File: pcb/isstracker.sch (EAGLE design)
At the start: 23 parts, among them IC1 74LS125N, J1 MOTOR_RIGHT, J2 CONTROL, J3 MOTOR_LEFT, J4 DISPLAY, J5 DEC_POSITION, J7 LED, J8 UART, J9 DISTANCE, U1 ARGON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

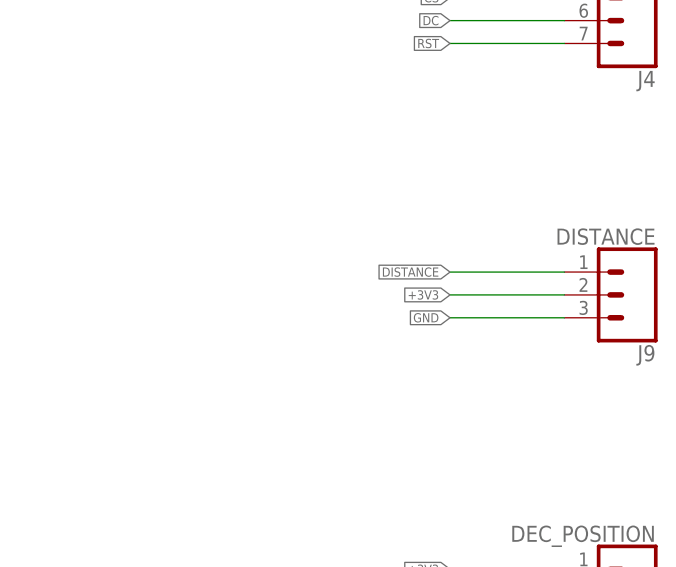
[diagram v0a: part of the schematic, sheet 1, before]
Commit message: Fixing PCB to use the new IR sensor instead.
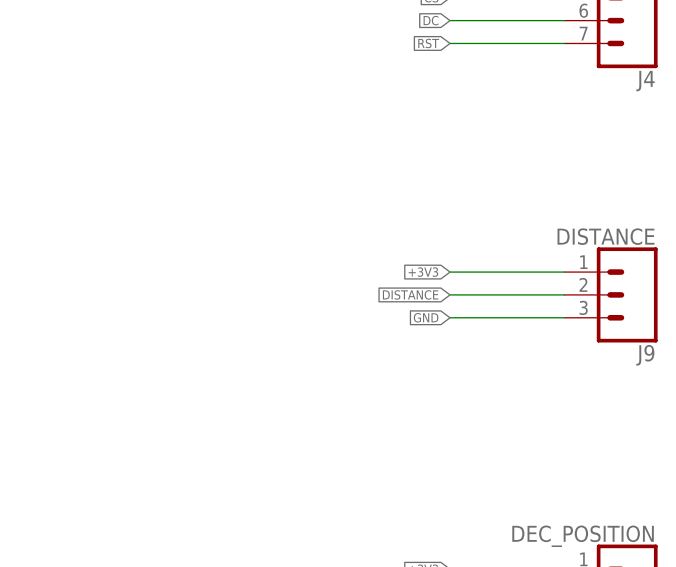
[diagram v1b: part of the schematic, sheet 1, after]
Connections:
- net +3V3: now also J9.1; no longer J9.2
- net DISTANCE: now also J9.2; no longer J9.1
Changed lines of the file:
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@@
 </segment>
 <segment>
-<wire x1="251.46" y1="147.32" x2="238.76" y2="147.32" width="0.1524" layer="91"/>
-<label x="238.76" y="147.32" size="1.016" layer="95" rot="R180" xref="yes"/>
-<pinref part="J9" gate="J$1" pin="2"/>
+<wire x1="251.46" y1="149.86" x2="238.76" y2="149.86" width="0.1524" layer="91"/>
+<label x="238.76" y="149.86" size="1.016" layer="95" rot="R180" xref="yes"/>
+<pinref part="J9" gate="J$1" pin="1"/>
 </segment>
 </net>
@@
 <net name="DISTANCE" class="0">
 <segment>
-<wire x1="251.46" y1="149.86" x2="238.76" y2="149.86" width="0.1524" layer="91"/>
-<label x="238.76" y="149.86" size="1.016" layer="95" rot="R180" xref="yes"/>
-<pinref part="J9" gate="J$1" pin="1"/>
-</segment>
-<segment>
 <pinref part="U1" gate="U1" pin="A2"/>
 <wire x1="124.46" y1="180.34" x2="114.3" y2="180.34" width="0.1524" layer="91"/>
 <label x="114.3" y="180.34" size="1.016" layer="95" rot="R180" xref="yes"/>
 </segment>
+<segment>
+<wire x1="251.46" y1="147.32" x2="238.76" y2="147.32" width="0.1524" layer="91"/>
+<label x="238.76" y="147.32" size="1.016" layer="95" rot="R180" xref="yes"/>
+<pinref part="J9" gate="J$1" pin="2"/>
+</segment>
 </net>

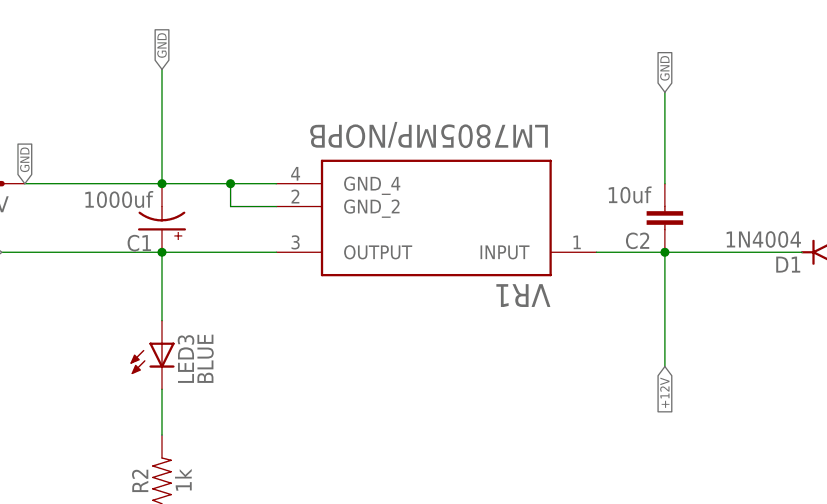
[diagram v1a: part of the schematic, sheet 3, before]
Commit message: Version 47:
* Only wake motor from sleep IFF we are going to move the motor
* Clean up some extra logging
* Add LED controls for the globe lighting
* This includes the first PCB sent out for production at OSHPark
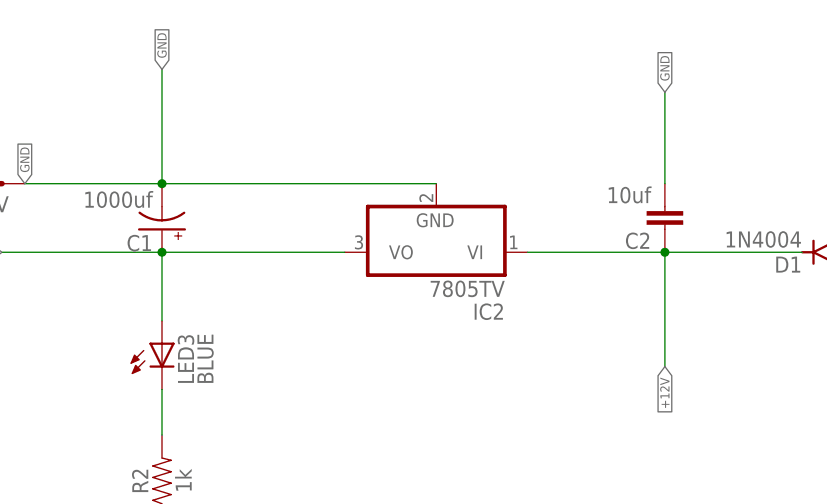
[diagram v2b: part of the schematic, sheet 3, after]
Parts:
- removed VR1: LM7805MP/NOPB, LM7805MP_NOPB:LM7805MP/NOPB
- added IC2: 7805TV, linear:7805TV
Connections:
- net +12V: now also IC2.VI; no longer VR1.INPUT
- net +5V: now also IC2.VO; no longer VR1.OUTPUT
- net GND: now also IC2.GND; no longer VR1.GND_2, VR1.GND_4
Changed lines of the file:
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@@
 <part name="R2" library="SparkFun-Resistors" library_urn="urn:adsk.eagle:library:532" deviceset="0.3OHM" device="-0805-1/8W-1%" package3d_urn="urn:adsk.eagle:package:39651/1" value="1k"/>
 <part name="J5" library="SparkFun-Connectors" library_urn="urn:adsk.eagle:library:513" deviceset="CONN_03" device="" package3d_urn="urn:adsk.eagle:package:38063/1" value="DEC_POSITION"/>
-<part name="VR1" library="LM7805MP_NOPB" deviceset="LM7805MP/NOPB" device=""/>
 <part name="C2" library="SparkFun-Capacitors" library_urn="urn:adsk.eagle:library:510" deviceset="1.0UF" device="-0805-25V-10%" package3d_urn="urn:adsk.eagle:package:37429/1" value="10uf"/>
 <part name="J4" library="SparkFun-Connectors" library_urn="urn:adsk.eagle:library:513" deviceset="CONN_07" device="" package3d_urn="urn:adsk.eagle:package:38129/1" value="DISPLAY"/>
@@
 <part name="H3" library="holes" library_urn="urn:adsk.eagle:library:237" deviceset="MOUNT-HOLE" device="3.0" package3d_urn="urn:adsk.eagle:package:14277/1"/>
 <part name="H4" library="holes" library_urn="urn:adsk.eagle:library:237" deviceset="MOUNT-HOLE" device="3.0" package3d_urn="urn:adsk.eagle:package:14277/1"/>
+<part name="IC2" library="linear" library_urn="urn:adsk.eagle:library:262" deviceset="78*" device="TV" package3d_urn="urn:adsk.eagle:package:16417/2" technology="05"/>
 </parts>
 <sheets>
@@
 <attribute name="VALUE" x="47.244" y="101.6" size="1.778" layer="96" font="vector" rot="R90" align="top-center"/>
 </instance>
-<instance part="VR1" gate="G$1" x="76.2" y="129.54" smashed="yes" rot="R180">
-<attribute name="NAME" x="88.9" y="123.46" size="2.54" layer="95" ratio="10" rot="SR180"/>
-<attribute name="VALUE" x="88.9" y="138.62" size="2.54" layer="96" ratio="10" rot="SR180" align="top-left"/>
-</instance>
 <instance part="C2" gate="G$1" x="101.6" y="132.08" smashed="yes" rot="R180">
 <attribute name="NAME" x="100.076" y="129.159" size="1.778" layer="95" font="vector" rot="R180"/>
@@
 <attribute name="NAME" x="116.84" y="126.5174" size="1.778" layer="95" rot="R180"/>
 <attribute name="VALUE" x="116.84" y="129.3114" size="1.778" layer="96" rot="R180"/>
+</instance>
+<instance part="IC2" gate="A1" x="76.2" y="127" smashed="yes" rot="R180">
+<attribute name="NAME" x="83.82" y="121.285" size="1.778" layer="95" rot="R180"/>
+<attribute name="VALUE" x="83.82" y="123.825" size="1.778" layer="96" rot="R180"/>
 </instance>
 </instances>
@@
 <net name="+5V" class="0">
 <segment>
-<pinref part="VR1" gate="G$1" pin="OUTPUT"/>
 <pinref part="C1" gate="G$1" pin="+"/>
-<wire x1="58.42" y1="127" x2="45.72" y2="127" width="0.1524" layer="91"/>
+<wire x1="66.04" y1="127" x2="45.72" y2="127" width="0.1524" layer="91"/>
 <wire x1="45.72" y1="127" x2="27.94" y2="127" width="0.1524" layer="91"/>
 <junction x="45.72" y="127"/>
@@
 <wire x1="45.72" y1="127" x2="45.72" y2="119.38" width="0.1524" layer="91"/>
 <label x="27.94" y="127" size="1.016" layer="95" rot="R180" xref="yes"/>
+<pinref part="IC2" gate="A1" pin="VO"/>
 </segment>
 </net>
 <net name="GND" class="0">
 <segment>
-<pinref part="VR1" gate="G$1" pin="GND_2"/>
-<wire x1="58.42" y1="132.08" x2="53.34" y2="132.08" width="0.1524" layer="91"/>
-<wire x1="53.34" y1="132.08" x2="53.34" y2="134.62" width="0.1524" layer="91"/>
 <pinref part="C1" gate="G$1" pin="-"/>
-<wire x1="53.34" y1="134.62" x2="45.72" y2="134.62" width="0.1524" layer="91"/>
-<pinref part="VR1" gate="G$1" pin="GND_4"/>
-<wire x1="58.42" y1="134.62" x2="53.34" y2="134.62" width="0.1524" layer="91"/>
-<junction x="53.34" y="134.62"/>
 <pinref part="X1" gate="-2" pin="S"/>
 <wire x1="45.72" y1="134.62" x2="30.48" y2="134.62" width="0.1524" layer="91"/>
@@
 <label x="45.72" y="147.32" size="1.016" layer="95" rot="R90" xref="yes"/>
 <label x="30.48" y="134.62" size="1.016" layer="95" rot="R90" xref="yes"/>
+<pinref part="IC2" gate="A1" pin="GND"/>
+<wire x1="45.72" y1="134.62" x2="76.2" y2="134.62" width="0.1524" layer="91"/>
 </segment>
 <segment>
@@
 <pinref part="C2" gate="G$1" pin="1"/>
 <wire x1="116.84" y1="127" x2="101.6" y2="127" width="0.1524" layer="91"/>
-<pinref part="VR1" gate="G$1" pin="INPUT"/>
-<wire x1="101.6" y1="127" x2="93.98" y2="127" width="0.1524" layer="91"/>
 <junction x="101.6" y="127"/>
 <wire x1="101.6" y1="127" x2="101.6" y2="114.3" width="0.1524" layer="91"/>
 <label x="101.6" y="114.3" size="1.016" layer="95" rot="R270" xref="yes"/>
-</segment>
-</net>
+<pinref part="IC2" gate="A1" pin="VI"/>
+<wire x1="101.6" y1="127" x2="86.36" y2="127" width="0.1524" layer="91"/>
+</segment>
+</net>

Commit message: Updating to the latest PCB to fix breaking issues
* Fixed capacitor sets for both boards to be larger and polarized on the
LDO's
* Fixed left track for motor board as it was 1 pin too short
* Switched from Declination to Azimuth
* Moved Azimuth signaling to the internal board to allow for movement
* Removed resistors on 5V LED signal buffer
* Switch LED pinout to match the Lumenati ordering
* Internal board got a polarized capacitor
* Internal board layout moved around to better match reality
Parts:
- removed J5: DEC_POSITION, SparkFun-Connectors:CONN_03
- removed R3: 300, SparkFun-Resistors:0.3OHM-0805-1/8W-1%
- added LED1: RED, adafruit:LED3MM
- C1: value 1000uf -> 100uF; device SparkFun-Capacitors:1000UF-RADIAL-5MM-25V-20% -> SparkFun-Capacitors:100UF-POLAR-RADIAL-2.5MM-25V-20%
- C2: value 10uf -> 100uF; device SparkFun-Capacitors:1.0UF-0805-25V-10% -> SparkFun-Capacitors:100UF-POLAR-RADIAL-2.5MM-25V-20%
- H1, H2, H3, H4: value MOUNT-HOLE3.0 -> STAND-OFF; device holes:MOUNT-HOLE3.0 -> SparkFun-Hardware:STAND-OFF
- IC1: value 74LS125N -> SN74AHCT125N; device adafruit:74LS125N -> adafruit:74125N
- IC2: value 7805TV -> L7805CV
- J2: value CONTROL -> MOTOR_LEFT; device SparkFun-Connectors:CONN_08" -> SparkFun-Connectors:CONN_11
- J3: value MOTOR_LEFT -> CONTROL; device SparkFun-Connectors:CONN_10" -> SparkFun-Connectors:CONN_08"
- R1: value 300 -> 1k
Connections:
- removed net DEC: J5.3, U1.A1
- removed net N$3: J7.1, R3.1
- new net AZIMUTH: J3.8, U1.A1
- net +12V: now also C2.+, R1.2; no longer C2.1
- net +3V3: no longer J5.1
- net +5V: now also J3.5; no longer J1.13, J1.14, J2.3
- net A+: now also J3.4; no longer J2.7
- net A-: now also J3.3; no longer J2.6
- net B+: now also J3.2; no longer J2.5
- net B-: now also J3.1; no longer J2.4
- net CO: now also IC1A.O, J7.2; no longer IC1D.O, R1.2
- net DO: now also IC1B.O, J7.3; no longer IC1C.O, R3.2
- net GND: now also C2.-, IC1C.O, IC1D.O, J2.3, J3.6, J7.1, LED1.C; no longer C2.2, IC1A.O, IC1B.O, J2.2, J3.3, J5.2, J7.3
- net LED_CO: now also IC1A.I; no longer IC1D.I
- net LED_DO: now also IC1B.I; no longer IC1C.I
- net MTR_DIR: now also J2.1; no longer J3.1
- net MTR_MS1: now also J2.10; no longer J3.9
- net MTR_SLP: now also J2.11; no longer J3.10
- net MTR_STEP: now also J2.2; no longer J3.2
- net N$2: now also LED1.A; no longer J7.2
- net SERVO: now also J3.7; no longer J2.8

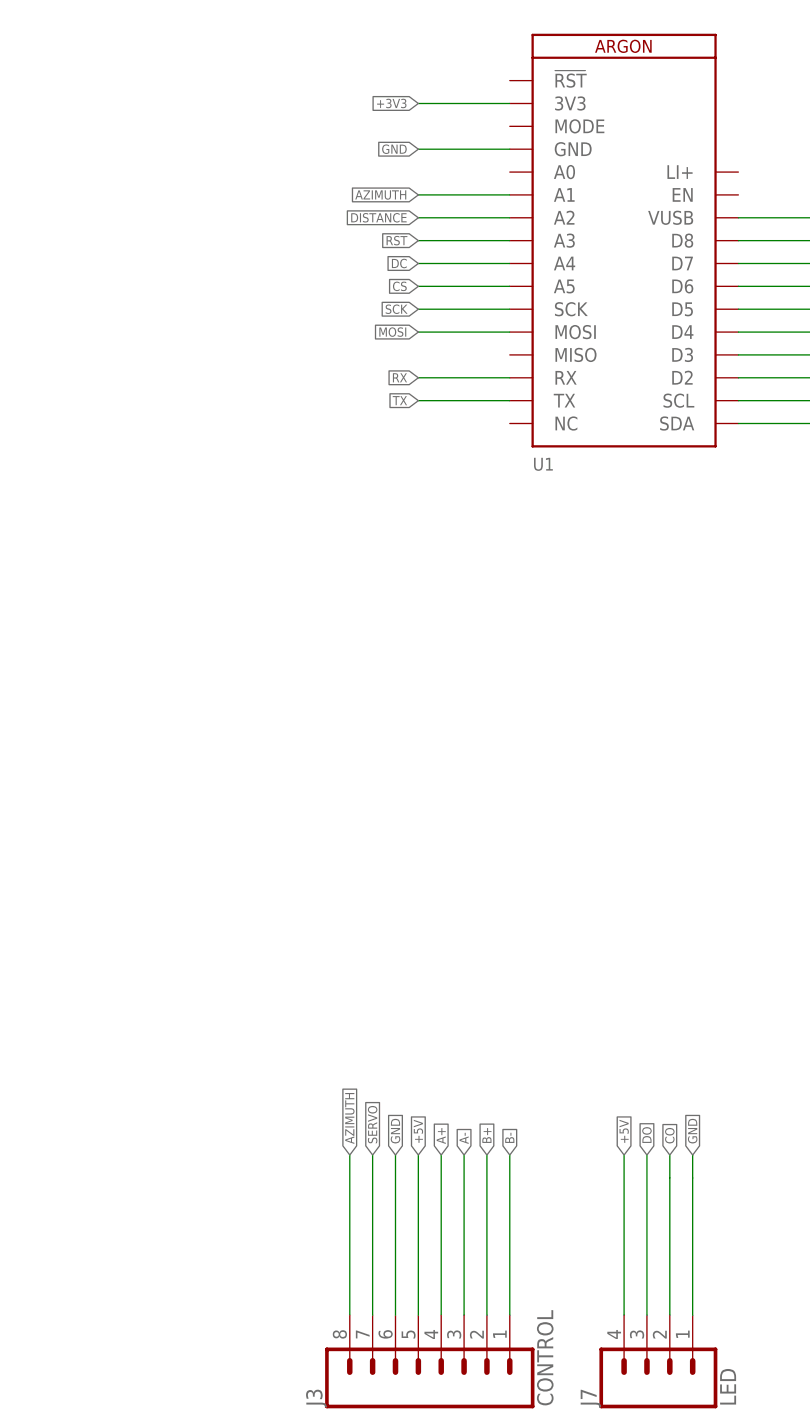
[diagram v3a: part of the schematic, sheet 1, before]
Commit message: Adding laser control
* Hookup an NPN to be able to turn the laser on/off via A0
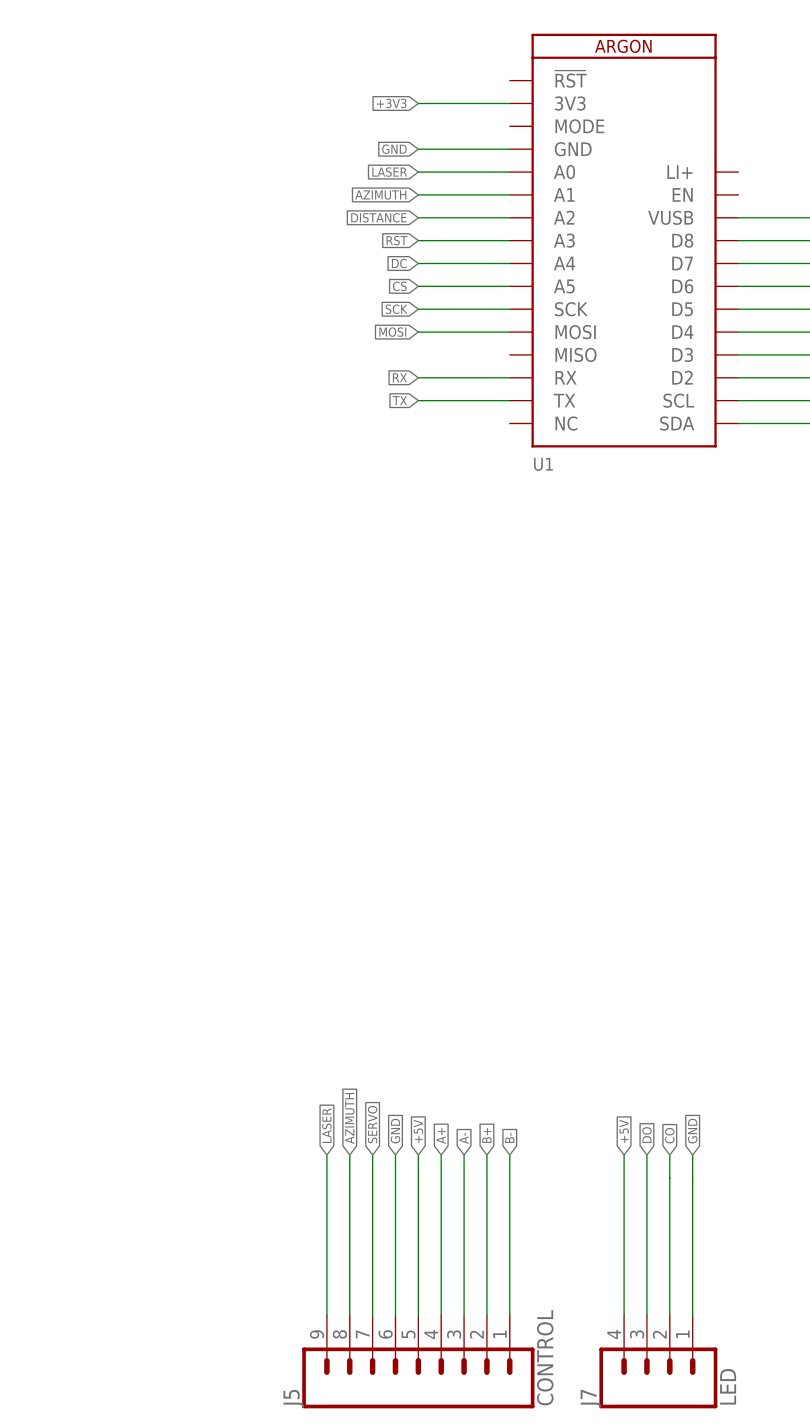
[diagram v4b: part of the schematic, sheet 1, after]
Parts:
- removed J3: CONTROL, SparkFun-Connectors:CONN_08"
- added J5: CONTROL, SparkFun-Connectors:CONN_09
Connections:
- new net LASER: J5.9, U1.A0
- net +5V: now also J5.5; no longer J3.5
- net A+: now also J5.4; no longer J3.4
- net A-: now also J5.3; no longer J3.3
- net AZIMUTH: now also J5.8; no longer J3.8
- net B+: now also J5.2; no longer J3.2
- net B-: now also J5.1; no longer J3.1
- net GND: now also J5.6; no longer J3.6
- net SERVO: now also J5.7; no longer J3.7
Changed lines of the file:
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@@
 <part name="H4" library="SparkFun-Hardware" library_urn="urn:adsk.eagle:library:519" deviceset="STAND-OFF" device="" package3d_urn="urn:adsk.eagle:package:38630/1"/>
 <part name="C2" library="SparkFun-Capacitors" library_urn="urn:adsk.eagle:library:510" deviceset="100UF-POLAR" device="-RADIAL-2.5MM-25V-20%" package3d_urn="urn:adsk.eagle:package:37415/1" value="100uF"/>
-<part name="J3" library="SparkFun-Connectors" library_urn="urn:adsk.eagle:library:513" deviceset="CONN_08" device="&quot;" package3d_urn="urn:adsk.eagle:package:38138/1" value="CONTROL"/>
 <part name="C1" library="SparkFun-Capacitors" library_urn="urn:adsk.eagle:library:510" deviceset="100UF-POLAR" device="-RADIAL-2.5MM-25V-20%" package3d_urn="urn:adsk.eagle:package:37415/1" value="100uF"/>
 <part name="H1" library="SparkFun-Hardware" library_urn="urn:adsk.eagle:library:519" deviceset="STAND-OFF" device="" package3d_urn="urn:adsk.eagle:package:38630/1"/>
 <part name="FRAME2" library="frames" library_urn="urn:adsk.eagle:library:229" deviceset="FRAME_A_L" device=""/>
 <part name="IC1" library="adafruit" library_urn="urn:adsk.eagle:library:420" deviceset="74*125" device="N" package3d_urn="urn:adsk.eagle:package:6240741/1" value="SN74AHCT125N"/>
+<part name="J5" library="SparkFun-Connectors" library_urn="urn:adsk.eagle:library:513" deviceset="CONN_09" device="" package3d_urn="urn:adsk.eagle:package:38153/1" value="CONTROL"/>
 </parts>
 <sheets>
@@
 <attribute name="NAME" x="10.16" y="163.068" size="1.778" layer="95" font="vector"/>
 </instance>
-<instance part="J3" gate="G$1" x="116.84" y="53.34" smashed="yes" rot="R90">
+<instance part="J5" gate="G$1" x="114.3" y="48.26" smashed="yes" rot="R90">
 <attribute name="VALUE" x="129.286" y="48.26" size="1.778" layer="96" font="vector" rot="R90"/>
-<attribute name="NAME" x="103.632" y="48.26" size="1.778" layer="95" font="vector" rot="R90"/>
+<attribute name="NAME" x="101.092" y="48.26" size="1.778" layer="95" font="vector" rot="R90"/>
 </instance>
 </instances>
@@
 <wire x1="109.22" y1="58.42" x2="109.22" y2="76.2" width="0.1524" layer="91"/>
 <label x="109.22" y="76.2" size="1.016" layer="95" rot="R90" xref="yes"/>
-<pinref part="J3" gate="G$1" pin="7"/>
+<pinref part="J5" gate="G$1" pin="7"/>
 </segment>
 </net>
@@
 <wire x1="116.84" y1="58.42" x2="116.84" y2="76.2" width="0.1524" layer="91"/>
 <label x="116.84" y="76.2" size="1.016" layer="95" rot="R90" xref="yes"/>
-<pinref part="J3" gate="G$1" pin="4"/>
+<pinref part="J5" gate="G$1" pin="4"/>
 </segment>
 </net>
@@
 <wire x1="119.38" y1="58.42" x2="119.38" y2="76.2" width="0.1524" layer="91"/>
 <label x="119.38" y="76.2" size="1.016" layer="95" rot="R90" xref="yes"/>
-<pinref part="J3" gate="G$1" pin="3"/>
+<pinref part="J5" gate="G$1" pin="3"/>
 </segment>
 </net>
@@
 <wire x1="121.92" y1="58.42" x2="121.92" y2="76.2" width="0.1524" layer="91"/>
 <label x="121.92" y="76.2" size="1.016" layer="95" rot="R90" xref="yes"/>
-<pinref part="J3" gate="G$1" pin="2"/>
+<pinref part="J5" gate="G$1" pin="2"/>
 </segment>
 </net>
@@
 <wire x1="124.46" y1="58.42" x2="124.46" y2="76.2" width="0.1524" layer="91"/>
 <label x="124.46" y="76.2" size="1.016" layer="95" rot="R90" xref="yes"/>
-<pinref part="J3" gate="G$1" pin="1"/>
+<pinref part="J5" gate="G$1" pin="1"/>
 </segment>
 </net>
@@
 <wire x1="111.76" y1="58.42" x2="111.76" y2="76.2" width="0.1524" layer="91"/>
 <label x="111.76" y="76.2" size="1.016" layer="95" rot="R90" xref="yes"/>
-<pinref part="J3" gate="G$1" pin="6"/>
+<pinref part="J5" gate="G$1" pin="6"/>
 </segment>
 </net>
@@
 <wire x1="114.3" y1="58.42" x2="114.3" y2="76.2" width="0.1524" layer="91"/>
 <label x="114.3" y="76.2" size="1.016" layer="95" rot="R90" xref="yes"/>
-<pinref part="J3" gate="G$1" pin="5"/>
+<pinref part="J5" gate="G$1" pin="5"/>
 </segment>
 </net>
@@
 <net name="AZIMUTH" class="0">
 <segment>
-<pinref part="J3" gate="G$1" pin="8"/>
 <wire x1="106.68" y1="58.42" x2="106.68" y2="76.2" width="0.1524" layer="91"/>
 <label x="106.68" y="76.2" size="1.016" layer="95" rot="R90" xref="yes"/>
+<pinref part="J5" gate="G$1" pin="8"/>
 </segment>
 <segment>
@@
 </segment>
 </net>
+<net name="LASER" class="0">
+<segment>
+<pinref part="J5" gate="G$1" pin="9"/>
+<wire x1="104.14" y1="58.42" x2="104.14" y2="76.2" width="0.1524" layer="91"/>
+<label x="104.14" y="76.2" size="1.016" layer="95" rot="R90" xref="yes"/>
+</segment>
+<segment>
+<pinref part="U1" gate="U1" pin="A0"/>
+<wire x1="124.46" y1="185.42" x2="114.3" y2="185.42" width="0.1524" layer="91"/>
+<label x="114.3" y="185.42" size="1.016" layer="95" rot="R180" xref="yes"/>
+</segment>
+</net>
